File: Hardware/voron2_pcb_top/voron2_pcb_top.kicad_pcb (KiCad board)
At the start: 2 copper layers, 77 x 60 mm, 19 parts, among them J1 bme280, J10 y_limit, J11 b_motor, J12 a_motor, J13 hotend_fan, J14 x_limit, J15 Conn_01x03, J2 Conn_01x04, J3 probe, J4 extruder, J5 Conn_02x06_Top_Bottom, J6 adxl345, J7 Conn_02x12_Top_Bottom, J8 thermistor, J9 part_fan

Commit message: Added Logo And JCLPCB Order Number Location
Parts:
- added G***: LOGO, Logo_footprint:logo_14mm, F.Cu at (98.5, 37.0)
- added G***: LOGO, Logo_footprint:logo_14mm, F.Cu at (137.2, 65.2)
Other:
- board text added: "JLCJLCJLCJLC"

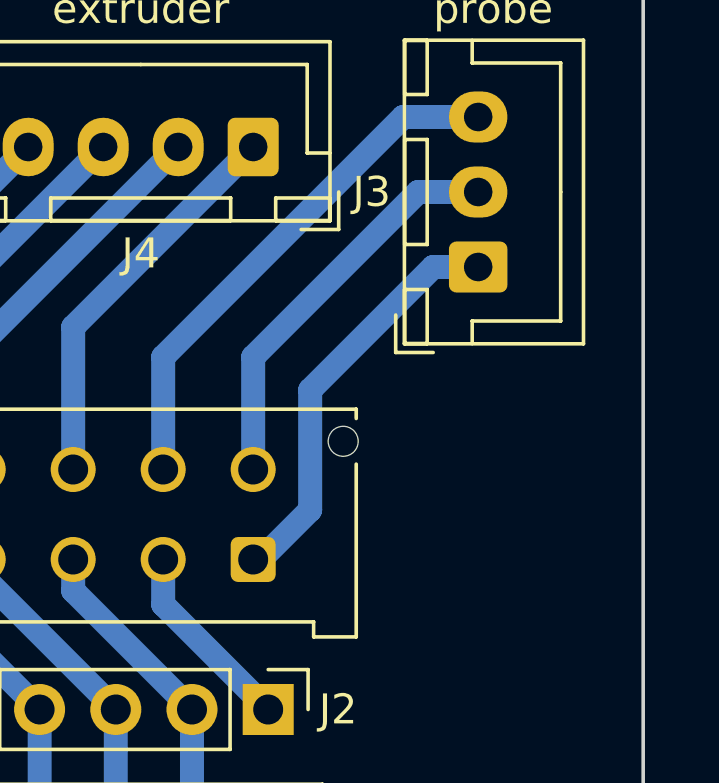
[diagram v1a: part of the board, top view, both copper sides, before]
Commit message: Added BAT85 diode to top breakoutboard in top only option.
Added rendered image of top option.
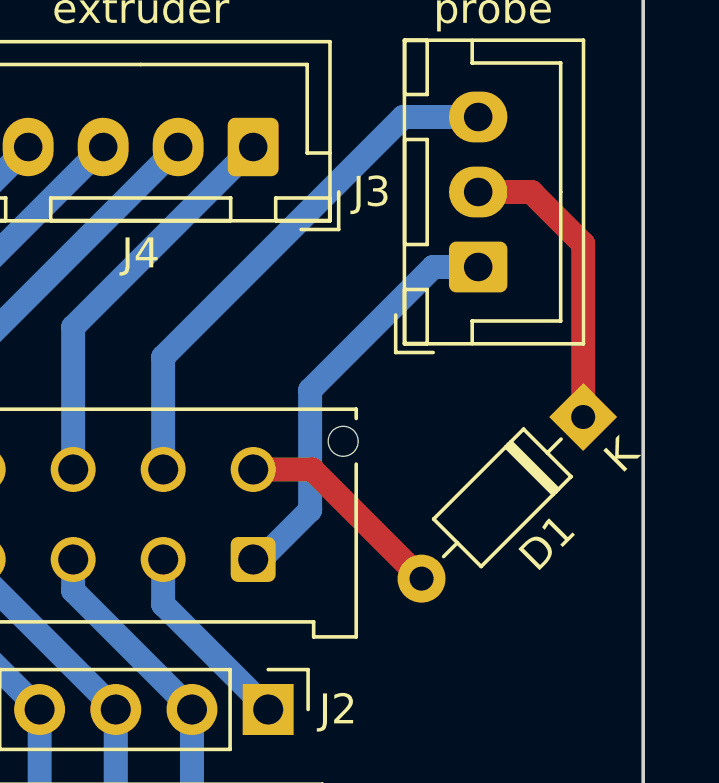
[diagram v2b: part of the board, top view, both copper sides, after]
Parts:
- added D1: BAT85, Diode_THT:D_DO-35_SOD27_P7.62mm_Horizontal, F.Cu at (161.0, 30.0)
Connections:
- J3 pad 2: Net-(J3-Pad2) -> Net-(D1-Pad1)
- J7 pad 13: Net-(J3-Pad2) -> Net-(D1-Pad2)
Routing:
- net Net-(J3-Pad2): track 13.5 -> 0.00 mm
- net Net-(D1-Pad1): track 0.00 -> 9.99 mm
- net Net-(D1-Pad2): track 0.00 -> 7.12 mm

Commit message: Separated top in top and back for easier production.
Added renders of top and back PCBs.
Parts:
- removed the G*** at (98.5, 37.0)
- removed the H1 at (91.0, 35.0)
- removed the H2 at (106.0, 35.0)
- removed the J1 at (102.2, 48.8)
- removed the J11 at (91.0, 72.0)
- removed J12: a_motor, Connector_JST:JST_XH_B4B-XH-A_1x04_P2.50mm_Vertical
- removed the J5 at (106.0, 58.5)
- renumbered H3 to H1, H4 to H2, J4 to J1, J6 to J10, J14 to J11, J8 to J2, J9 to J4, J13 to J5, J7 to J6, J2 to J7, J15 to J8, J10 to J9
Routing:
- net Net-(J11-Pad1) (its old number): track 18.2 -> 0.00 mm
- net Net-(J12-Pad4): track 18.0 -> 0.00 mm
- net Net-(J12-Pad3): track 13.4 -> 0.00 mm
- net Net-(J11-Pad2) (its old number): track 13.4 -> 0.00 mm
- net Net-(J11-Pad4): track 11.7 -> 0.00 mm
- net Net-(J12-Pad1): track 11.1 -> 0.00 mm
- net Net-(J12-Pad2): track 10.5 -> 0.00 mm
- net Net-(J11-Pad3): track 10.2 -> 0.00 mm
- net Net-(J1-Pad4) (its old number): track 7.06 -> 0.00 mm
- net Net-(J1-Pad1) (its old number): track 7.06 -> 0.00 mm
- net Net-(J1-Pad3) (its old number): track 6.85 -> 0.00 mm
- net Net-(J1-Pad2) (its old number): track 6.85 -> 0.00 mm
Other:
- board size 77 x 60 mm -> 50 x 60 mm
